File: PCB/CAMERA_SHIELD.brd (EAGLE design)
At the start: 79.7 x 100.3 mm, 73 parts, among them IC4 LSF0204PWR, J1 47346-0001, Q1 FDN304P, Q2 FDN304P, Q3 SSM3J338R,LF, Q4 SSM3J338R,LF, Q5 FDN304P, U1 LARA-R2

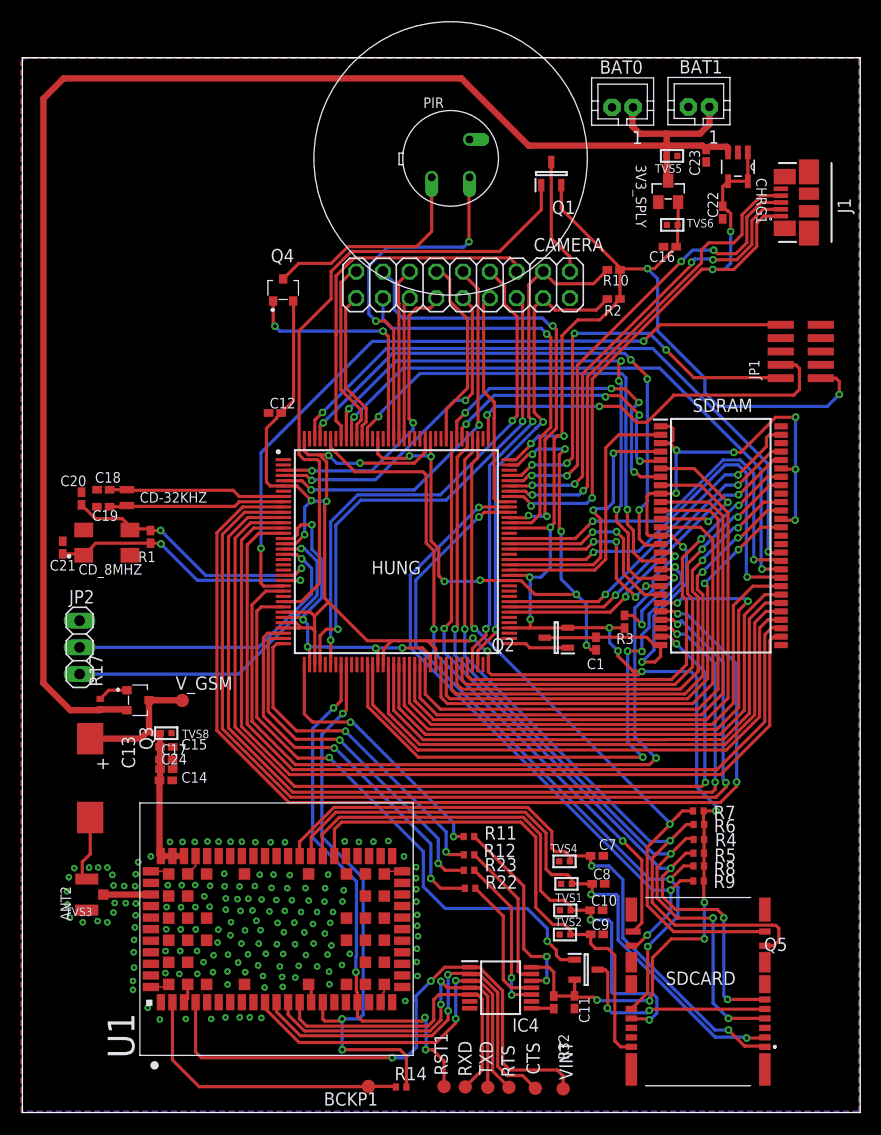
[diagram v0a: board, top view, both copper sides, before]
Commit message: fix power-pins
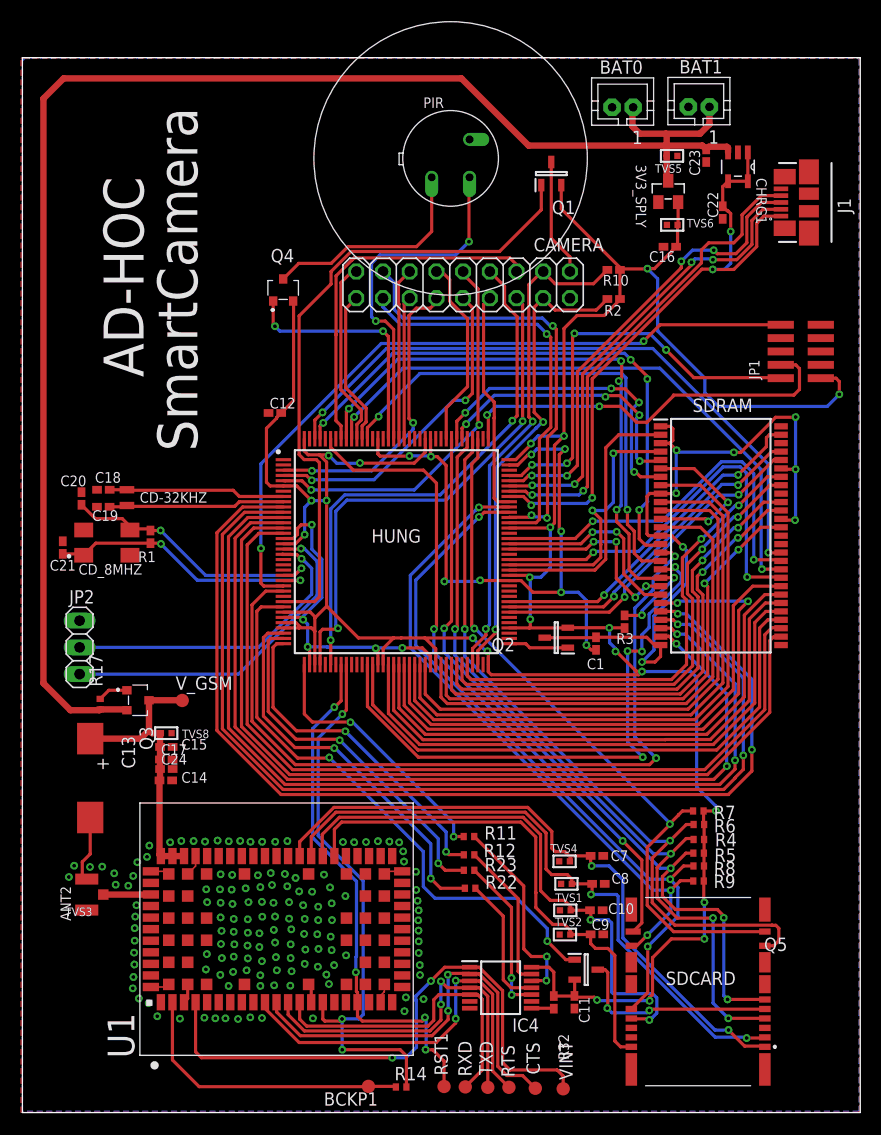
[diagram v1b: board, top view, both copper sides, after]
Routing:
- net FMC_A3: track 86.6 -> 88.0 mm
- net FMC_SDNE1: track 63.9 -> 62.8 mm
- net FMC_A10: track 56.6 -> 55.6 mm
- net DCMI_HSYNC: track 48.6 -> 49.6 mm
- net FMC_A2: track 91.6 -> 92.6 mm
- net FMC_A11: track 50.7 -> 50.0 mm
- net FMC_A9: track 52.3 -> 51.6 mm
- net FMC_A4: track 85.6 -> 84.8 mm
- net FMC_A8: track 53.0 -> 52.3 mm
- net DCMI_PIXCK: track 50.4 -> 51.1 mm
- net MOSFET_CAMERA: track 61.4 -> 62.1 mm
- net FMC_A1: track 96.1 -> 96.8 mm
- net FMC_A5: track 84.0 -> 83.3 mm
- net FMC_A7: track 53.6 -> 52.9 mm
- net FMC_D4: track 60.0 -> 59.3 mm
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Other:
- board text added: "AD-HOC"
- board text added: "SmartCamera"
